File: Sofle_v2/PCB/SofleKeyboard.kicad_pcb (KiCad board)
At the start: 2 copper layers, 143.5 x 115.5 mm, 89 parts, among them J1 LED, J2 4PIN, J3 OLED, SW1 SW_PUSH, SW10 SW_PUSH, SW11 SW_PUSH, SW12 SW_PUSH, SW13 SW_PUSH, SW14 SW_PUSH, SW15 SW_PUSH, SW16 SW_PUSH, SW17 SW_PUSH, SW18 SW_PUSH, SW19 SW_PUSH, SW2 SW_PUSH, SW20 SW_PUSH, SW21 SW_PUSH, SW22 SW_PUSH, SW23 SW_PUSH, SW24 SW_PUSH, SW25 Rotary_Encoder_Switch, SW26 SW_PUSH, SW27 SW_PUSH, SW28 SW_PUSH, SW29 SW_PUSH, SW3 SW_PUSH, SW30 SW_PUSH, SW4 SW_PUSH, SW5 SW_PUSH, SW6 SW_PUSH, SW7 SW_PUSH, SW8 SW_PUSH, SW9 SW_PUSH, U1 ProMicro

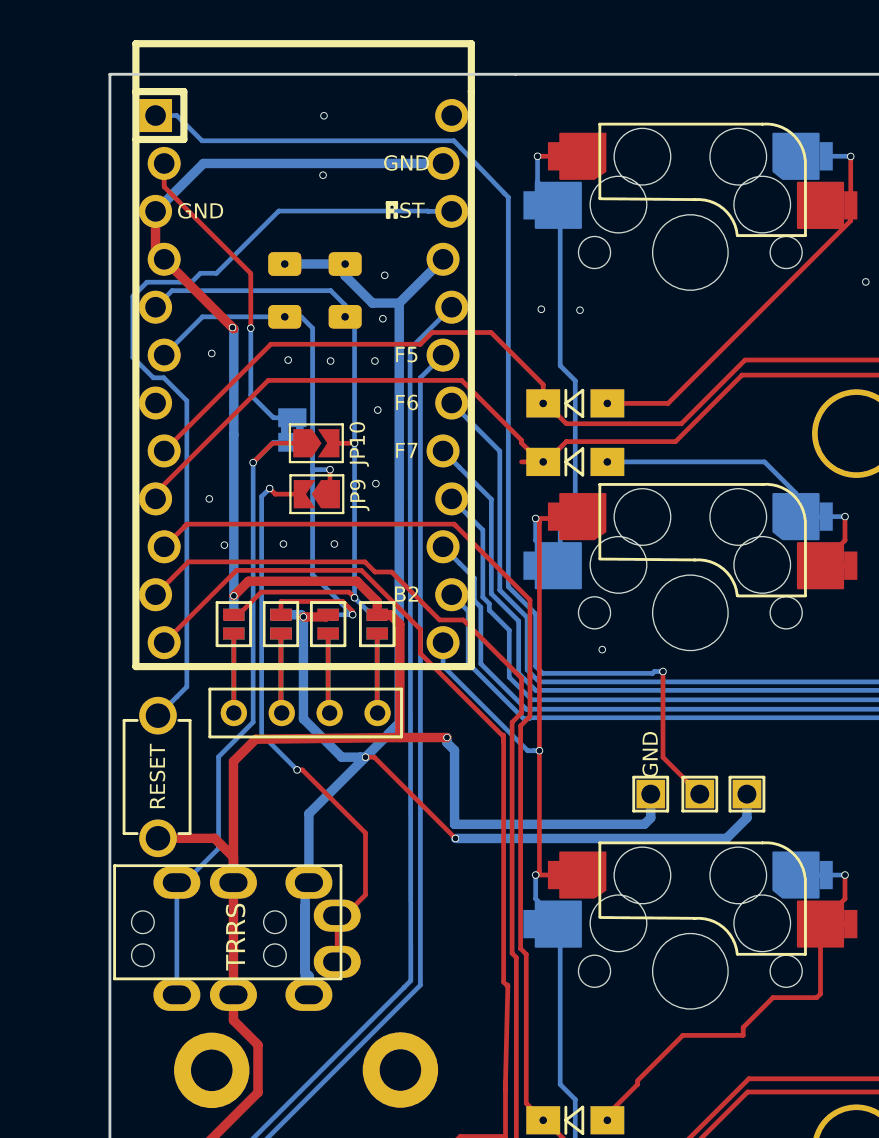
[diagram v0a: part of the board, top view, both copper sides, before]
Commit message: updates to use with nice-nano board
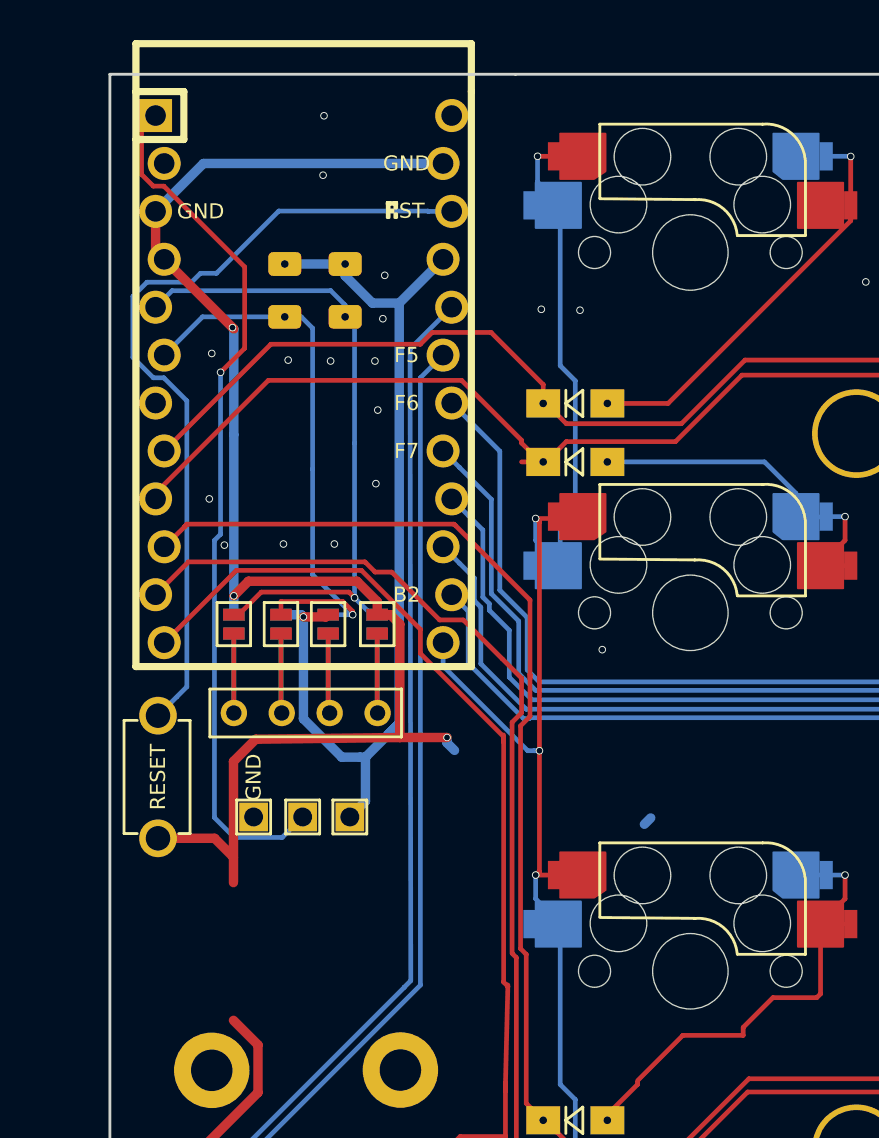
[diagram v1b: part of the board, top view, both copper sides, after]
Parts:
- removed J2: 4PIN, SofleKeyboard-footprint:MJ-4PP-9
- removed JP10: IC2SDA, Jumper:SolderJumper-2_P1.3mm_Open_TrianglePad1.0x1.5mm
- removed JP11: Serial, Jumper:SolderJumper-2_P1.3mm_Bridged2Bar_Pad1.0x1.5mm
- removed JP9: I2CSCL, Jumper:SolderJumper-2_P1.3mm_Open_TrianglePad1.0x1.5mm
- moved J1 21.1 mm to (102.5, 79.9)
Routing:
- net VCC: track 90.9 -> 51.9 mm, vias 3 -> 1
- net /i2c_d: track 35.7 -> 0.00 mm, vias 1 -> 0
- net /i2c_c: track 30.5 -> 0.00 mm, vias 2 -> 0
- net GND: track 122.6 -> 98.7 mm
- net DATA: track 16.9 -> 0.00 mm, vias 1 -> 0
- net LED: track 60.2 -> 46.3 mm
- net SCL: track 33.5 -> 31.2 mm, vias 2 -> 1
- net SDA: track 36.0 -> 34.7 mm, vias 2 -> 1
